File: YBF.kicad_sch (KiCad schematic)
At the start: 6 parts, among them J1 Chain_LED_out, J2 Chain_LED_return

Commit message: progress
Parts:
- removed U3: ~, pfornage-kicad-lib:ADA6066_Pixel_Shifter, symbol pfornage-kicad-lib:ADA6066_Pixel_Shifter
- added C53, C60: WCAP-ASLI_4X5.5, pfornage-kicad-lib:WCAP-ASLI_4X5.5_DXL_, symbol pfornage-kicad-lib:WCAP-ASLI_4X5.5
- added C54, C55, C56, C57, C58, C59: 1uF, Capacitor_SMD:C_0603_1608Metric, symbol Device:C
- added JP1: SolderJumper_3_Open, Jumper:SolderJumper-3_P1.3mm_Open_RoundedPad1.0x1.5mm_NumberLabels, symbol Jumper:SolderJumper_3_Open
- added S1: EG1224, pfornage-kicad-lib:SW_EG1224, symbol pfornage-kicad-lib:EG1224
- added SW1, SW2: 1825910-6, pfornage-kicad-lib:SW_1825910-6-4, symbol pfornage-kicad-lib:1825910-6
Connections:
- net +3.3V: now also C57.1
- net +5V: now also C53.1, C56.1, JP1.1 (A); no longer J1.1 (Pin_1), J2.1 (Pin_1)
- net +BATT: now also C59.1, C60.1, JP1.3 (B)
- net GND: now also C53.2, C54.2, C55.2, C56.2, C57.2, C58.2, C59.2, C60.2, S1.2, S1.S1 (SHIELD), S1.S2 (SHIELD__1), S1.S3 (SHIELD__2), S1.S4 (SHIELD__3), SW1.3, SW1.4, SW2.3, SW2.4
- net Perimeter LEDs/DIN: now also U1.5 (12)
- net at U1.10 (14): now also U2.5 (LRCL)
- net at U1.12 (SDA): no longer U2.4 (DOUT)
- net at U1.13 (37): now also C54.1, SW2.1, SW2.2
- net ~{DISABLE}: now reaches U1.2 (EN)
- net ~{DISABLE}: now also U4.4 (EN), C58.1, S1.1
- net at U1.6 (27): now also C55.1, SW1.1, SW1.2
- net at U1.8 (15): now also U2.4 (DOUT)
- new net Vdrive: J1.1 (Pin_1), J2.1 (Pin_1), JP1.2 (C)
- no-connect marks 2 -> 1
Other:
- moved on the sheet: J1, J2

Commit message: Hieracrchical PCB
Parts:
- renumbered C60 to C1, C53 to C2, C55 to C3, C59 to C4, C56 to C5, C58 to C6, C57 to C7, C54 to C8, U4 to U1, U1 to U2, U2 to U3
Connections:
- net DATA_CHAIN_OUT renamed PERIM_LED_DATA_IN
- net Perimeter LEDs/DIN renamed PERIM_LED_DATA_OUT
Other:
- removed sheet Perimeter LEDs
- added sheet ws2812_and_cap (ws2812_and_cap.kicad_sch)
- added sheet ws2812_and_cap1 (ws2812_and_cap.kicad_sch)
- added sheet ws2812_and_cap10 (ws2812_and_cap.kicad_sch)
- added sheet ws2812_and_cap11 (ws2812_and_cap.kicad_sch)
- added sheet ws2812_and_cap12 (ws2812_and_cap.kicad_sch)
- added sheet ws2812_and_cap13 (ws2812_and_cap.kicad_sch)
- added sheet ws2812_and_cap14 (ws2812_and_cap.kicad_sch)
- added sheet ws2812_and_cap15 (ws2812_and_cap.kicad_sch)
- added sheet ws2812_and_cap16 (ws2812_and_cap.kicad_sch)
- added sheet ws2812_and_cap17 (ws2812_and_cap.kicad_sch)
- added sheet ws2812_and_cap18 (ws2812_and_cap.kicad_sch)
- added sheet ws2812_and_cap19 (ws2812_and_cap.kicad_sch)
- added sheet ws2812_and_cap2 (ws2812_and_cap.kicad_sch)
- added sheet ws2812_and_cap20 (ws2812_and_cap.kicad_sch)
- added sheet ws2812_and_cap21 (ws2812_and_cap.kicad_sch)
- added sheet ws2812_and_cap22 (ws2812_and_cap.kicad_sch)
- added sheet ws2812_and_cap23 (ws2812_and_cap.kicad_sch)
- added sheet ws2812_and_cap24 (ws2812_and_cap.kicad_sch)
- added sheet ws2812_and_cap25 (ws2812_and_cap.kicad_sch)
- added sheet ws2812_and_cap26 (ws2812_and_cap.kicad_sch)
- added sheet ws2812_and_cap27 (ws2812_and_cap.kicad_sch)
- added sheet ws2812_and_cap28 (ws2812_and_cap.kicad_sch)
- added sheet ws2812_and_cap29 (ws2812_and_cap.kicad_sch)
- added sheet ws2812_and_cap3 (ws2812_and_cap.kicad_sch)
- added sheet ws2812_and_cap30 (ws2812_and_cap.kicad_sch)
- added sheet ws2812_and_cap31 (ws2812_and_cap.kicad_sch)
- added sheet ws2812_and_cap32 (ws2812_and_cap.kicad_sch)
- added sheet ws2812_and_cap33 (ws2812_and_cap.kicad_sch)
- added sheet ws2812_and_cap34 (ws2812_and_cap.kicad_sch)
- added sheet ws2812_and_cap35 (ws2812_and_cap.kicad_sch)
- added sheet ws2812_and_cap36 (ws2812_and_cap.kicad_sch)
- added sheet ws2812_and_cap37 (ws2812_and_cap.kicad_sch)
- added sheet ws2812_and_cap38 (ws2812_and_cap.kicad_sch)
- added sheet ws2812_and_cap39 (ws2812_and_cap.kicad_sch)
- added sheet ws2812_and_cap4 (ws2812_and_cap.kicad_sch)
- added sheet ws2812_and_cap40 (ws2812_and_cap.kicad_sch)
- added sheet ws2812_and_cap41 (ws2812_and_cap.kicad_sch)
- added sheet ws2812_and_cap42 (ws2812_and_cap.kicad_sch)
- added sheet ws2812_and_cap43 (ws2812_and_cap.kicad_sch)
- added sheet ws2812_and_cap44 (ws2812_and_cap.kicad_sch)
- added sheet ws2812_and_cap45 (ws2812_and_cap.kicad_sch)
- added sheet ws2812_and_cap46 (ws2812_and_cap.kicad_sch)
- added sheet ws2812_and_cap47 (ws2812_and_cap.kicad_sch)
- added sheet ws2812_and_cap48 (ws2812_and_cap.kicad_sch)
- added sheet ws2812_and_cap49 (ws2812_and_cap.kicad_sch)
- added sheet ws2812_and_cap5 (ws2812_and_cap.kicad_sch)
- added sheet ws2812_and_cap50 (ws2812_and_cap.kicad_sch)
- added sheet ws2812_and_cap51 (ws2812_and_cap.kicad_sch)
- added sheet ws2812_and_cap52 (ws2812_and_cap.kicad_sch)
- added sheet ws2812_and_cap53 (ws2812_and_cap.kicad_sch)
- added sheet ws2812_and_cap54 (ws2812_and_cap.kicad_sch)
- added sheet ws2812_and_cap55 (ws2812_and_cap.kicad_sch)
- added sheet ws2812_and_cap56 (ws2812_and_cap.kicad_sch)
- added sheet ws2812_and_cap57 (ws2812_and_cap.kicad_sch)
- added sheet ws2812_and_cap58 (ws2812_and_cap.kicad_sch)
- added sheet ws2812_and_cap59 (ws2812_and_cap.kicad_sch)
- added sheet ws2812_and_cap6 (ws2812_and_cap.kicad_sch)
- added sheet ws2812_and_cap60 (ws2812_and_cap.kicad_sch)
- added sheet ws2812_and_cap61 (ws2812_and_cap.kicad_sch)
- added sheet ws2812_and_cap62 (ws2812_and_cap.kicad_sch)
- added sheet ws2812_and_cap63 (ws2812_and_cap.kicad_sch)
- added sheet ws2812_and_cap64 (ws2812_and_cap.kicad_sch)
- added sheet ws2812_and_cap65 (ws2812_and_cap.kicad_sch)
- added sheet ws2812_and_cap66 (ws2812_and_cap.kicad_sch)
- added sheet ws2812_and_cap67 (ws2812_and_cap.kicad_sch)
- added sheet ws2812_and_cap68 (ws2812_and_cap.kicad_sch)
- added sheet ws2812_and_cap69 (ws2812_and_cap.kicad_sch)
- added sheet ws2812_and_cap7 (ws2812_and_cap.kicad_sch)
- added sheet ws2812_and_cap70 (ws2812_and_cap.kicad_sch)
- added sheet ws2812_and_cap71 (ws2812_and_cap.kicad_sch)
- added sheet ws2812_and_cap72 (ws2812_and_cap.kicad_sch)
- added sheet ws2812_and_cap73 (ws2812_and_cap.kicad_sch)
- added sheet ws2812_and_cap74 (ws2812_and_cap.kicad_sch)
- added sheet ws2812_and_cap75 (ws2812_and_cap.kicad_sch)
- added sheet ws2812_and_cap76 (ws2812_and_cap.kicad_sch)
- added sheet ws2812_and_cap77 (ws2812_and_cap.kicad_sch)
- added sheet ws2812_and_cap78 (ws2812_and_cap.kicad_sch)
- added sheet ws2812_and_cap79 (ws2812_and_cap.kicad_sch)
- added sheet ws2812_and_cap8 (ws2812_and_cap.kicad_sch)
- added sheet ws2812_and_cap80 (ws2812_and_cap.kicad_sch)
- added sheet ws2812_and_cap81 (ws2812_and_cap.kicad_sch)
- added sheet ws2812_and_cap82 (ws2812_and_cap.kicad_sch)
- added sheet ws2812_and_cap83 (ws2812_and_cap.kicad_sch)
- added sheet ws2812_and_cap84 (ws2812_and_cap.kicad_sch)
- added sheet ws2812_and_cap85 (ws2812_and_cap.kicad_sch)
- added sheet ws2812_and_cap86 (ws2812_and_cap.kicad_sch)
- added sheet ws2812_and_cap87 (ws2812_and_cap.kicad_sch)
- added sheet ws2812_and_cap88 (ws2812_and_cap.kicad_sch)
- added sheet ws2812_and_cap89 (ws2812_and_cap.kicad_sch)
- added sheet ws2812_and_cap9 (ws2812_and_cap.kicad_sch)
- added sheet ws2812_and_cap90 (ws2812_and_cap.kicad_sch)
- added sheet ws2812_and_cap91 (ws2812_and_cap.kicad_sch)
- added sheet ws2812_and_cap92 (ws2812_and_cap.kicad_sch)
- added sheet ws2812_and_cap93 (ws2812_and_cap.kicad_sch)
- added sheet ws2812_and_cap94 (ws2812_and_cap.kicad_sch)
- added sheet ws2812_and_cap95 (ws2812_and_cap.kicad_sch)
- moved on the sheet: C1, C2, C3, C4, C5, C6, C7, C8, J1, J2, JP1, S1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

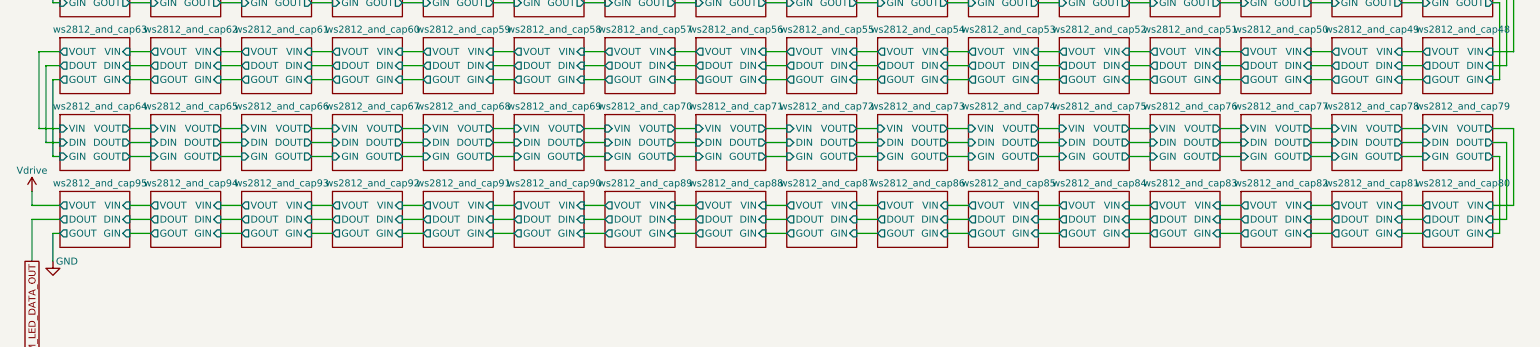
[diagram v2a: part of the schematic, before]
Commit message: place perim LEDs
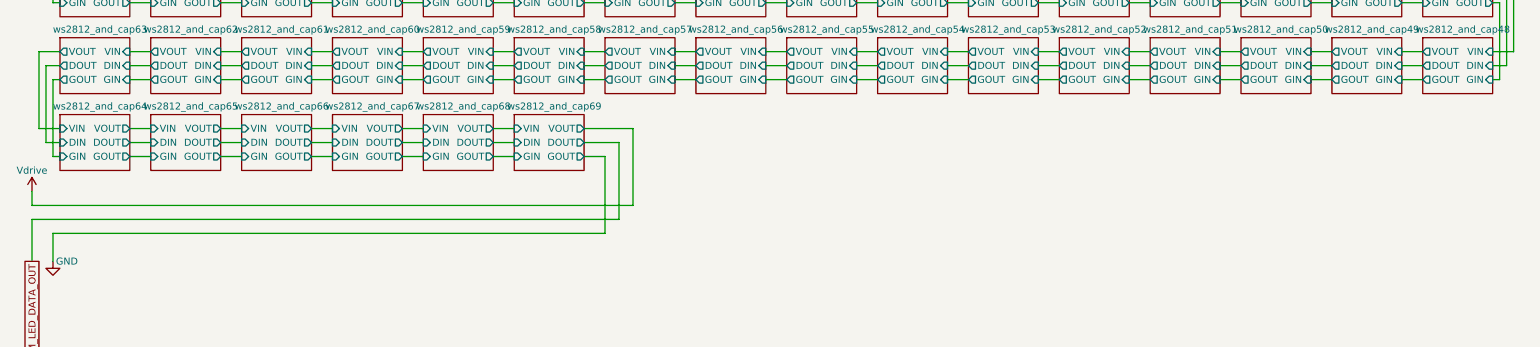
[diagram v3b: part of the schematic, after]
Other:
- removed sheet ws2812_and_cap70
- removed sheet ws2812_and_cap71
- removed sheet ws2812_and_cap72
- removed sheet ws2812_and_cap73
- removed sheet ws2812_and_cap74
- removed sheet ws2812_and_cap75
- removed sheet ws2812_and_cap76
- removed sheet ws2812_and_cap77
- removed sheet ws2812_and_cap78
- removed sheet ws2812_and_cap79
- removed sheet ws2812_and_cap80
- removed sheet ws2812_and_cap81
- removed sheet ws2812_and_cap82
- removed sheet ws2812_and_cap83
- removed sheet ws2812_and_cap84
- removed sheet ws2812_and_cap85
- removed sheet ws2812_and_cap86
- removed sheet ws2812_and_cap87
- removed sheet ws2812_and_cap88
- removed sheet ws2812_and_cap89
- removed sheet ws2812_and_cap90
- removed sheet ws2812_and_cap91
- removed sheet ws2812_and_cap92
- removed sheet ws2812_and_cap93
- removed sheet ws2812_and_cap94
- removed sheet ws2812_and_cap95

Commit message: v0.0.1
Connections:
- net PERIM_LED_DATA_IN: now also U2.5 (12); no longer J1.2 (Pin_2)
- net PERIM_LED_DATA_OUT: now also J1.2 (Pin_2); no longer U2.5 (12)
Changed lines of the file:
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@@
 	(global_label "PERIM_LED_DATA_IN"
 		(shape output)
-		(at 54.61 153.67 0)
-		(fields_autoplaced yes)
-		(effects
-			(font
-				(size 1.27 1.27)
-			)
-			(justify left)
-		)
-		(property "Intersheetrefs" "${INTERSHEET_REFS}"
-			(at 76.0404 153.67 0)
-			(effects
-				(font
-					(size 1.27 1.27)
-				)
-				(justify left)
-				(hide yes)
-			)
-		)
-	)
-	(global_label "PERIM_LED_DATA_OUT"
-		(shape input)
 		(at 148.59 172.72 270)
 		(fields_autoplaced yes)
@@
 		)
 		(property "Intersheetrefs" "${INTERSHEET_REFS}"
-			(at 148.59 195.8437 90)
+			(at 148.59 194.1504 90)
 			(effects
 				(font
@@
 				(hide yes)
 			)
+		)
+	)
+	(global_label "PERIM_LED_DATA_OUT"
+		(shape input)
+		(at 54.61 153.67 0)
+		(fields_autoplaced yes)
+		(effects
+			(font
+				(size 1.27 1.27)
+			)
+			(justify left)
+		)
+		(property "Intersheetrefs" "${INTERSHEET_REFS}"
+			(at 77.7337 153.67 0)
+			(effects
+				(font
+					(size 1.27 1.27)
+				)
+				(justify left)
+				(hide yes)
+			)

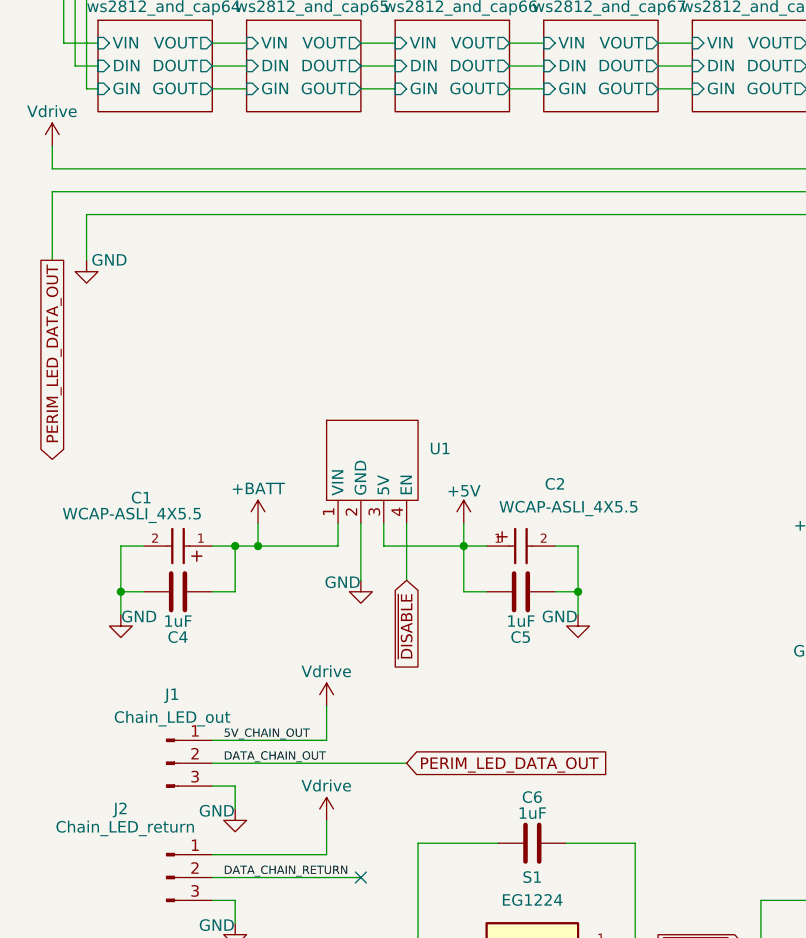
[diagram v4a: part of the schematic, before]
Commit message: v0.0.2
add mounting holes and seperate chain and perim led lines
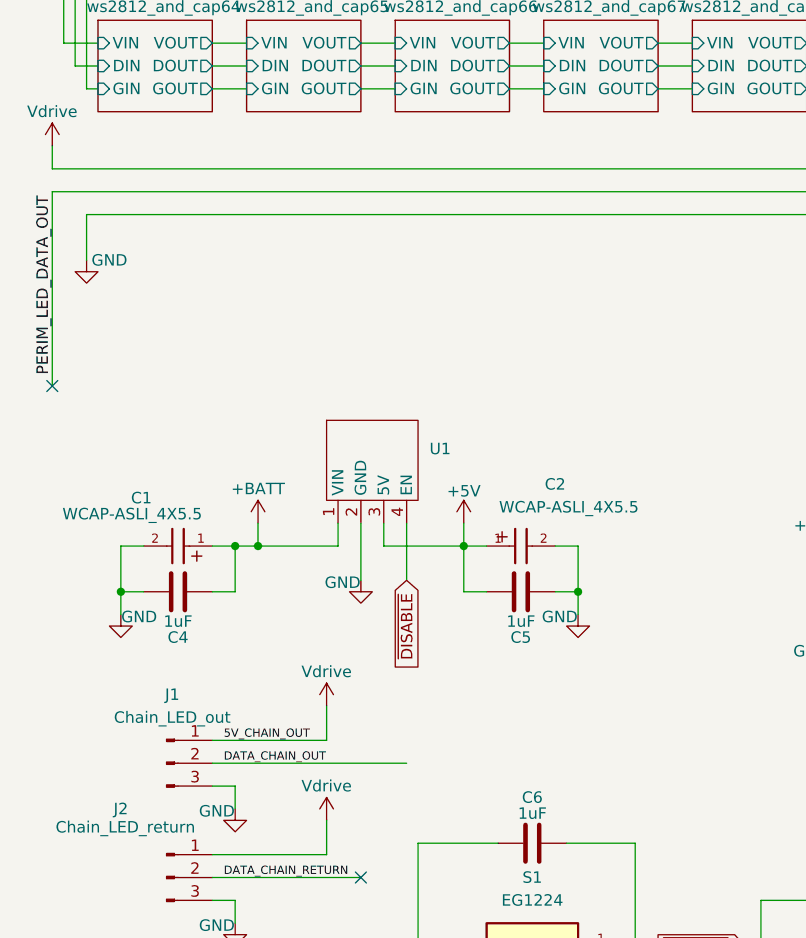
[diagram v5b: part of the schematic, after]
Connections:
- net PERIM_LED_DATA_OUT: no longer J1.2 (Pin_2)
- new net DATA_CHAIN_OUT: J1.2 (Pin_2)
- no-connect marks 1 -> 2
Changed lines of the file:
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@@
 	)
 	(no_connect
+		(at 15.24 111.76)
+	)
+	(no_connect
 		(at 49.53 166.37)
 	)
@@
 	(wire
 		(pts
+			(xy 15.24 90.17) (xy 15.24 111.76)
+		)
+		(stroke
+			(width 0)
+			(type default)
+		)
+	)
+	(wire
+		(pts
 			(xy 283.21 20.32) (xy 283.21 34.29)
 		)
@@
 	(wire
 		(pts
-			(xy 15.24 90.17) (xy 15.24 97.79)
-		)
-		(stroke
-			(width 0)
-			(type default)
-		)
-	)
-	(wire
-		(pts
 			(xy 156.21 170.18) (xy 156.21 156.21)
 		)
@@
 		)
 	)
+	(label "PERIM_LED_DATA_OUT"
+		(at 15.24 110.49 90)
+		(effects
+			(font
+				(size 1.27 1.27)
+			)
+			(justify left bottom)
+		)
+	)
 	(label "DATA_CHAIN_RETURN"
 		(at 34.29 166.37 0)
@@
 				(hide yes)
 			)
-		)
-	)
-	(global_label "PERIM_LED_DATA_OUT"
-		(shape output)
-		(at 15.24 97.79 270)
-		(fields_autoplaced yes)
-		(effects
-			(font
-				(size 1.27 1.27)
-			)
-			(justify right)
-		)
-		(property "Intersheetrefs" "${INTERSHEET_REFS}"
-			(at 15.24 120.9137 90)
-			(effects
-				(font
-					(size 1.27 1.27)
-				)
-				(justify right)
-				(hide yes)
-			)
-		)
-	)
-	(global_label "PERIM_LED_DATA_OUT"
-		(shape input)
-		(at 54.61 153.67 0)
-		(fields_autoplaced yes)
-		(effects
-			(font
-				(size 1.27 1.27)
-			)
-			(justify left)
-		)
-		(property "Intersheetrefs" "${INTERSHEET_REFS}"
-			(at 77.7337 153.67 0)
-			(effects
-				(font
-					(size 1.27 1.27)
-				)
-				(justify left)
-				(hide yes)
-			)
